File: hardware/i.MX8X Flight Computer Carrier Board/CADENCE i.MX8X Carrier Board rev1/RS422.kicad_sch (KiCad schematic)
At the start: 16 parts, among them CN1 DF11-16DP-2DSA(08), U18 MAX3485, U19 SN65C1168ERGYR, U20 P82B715DR

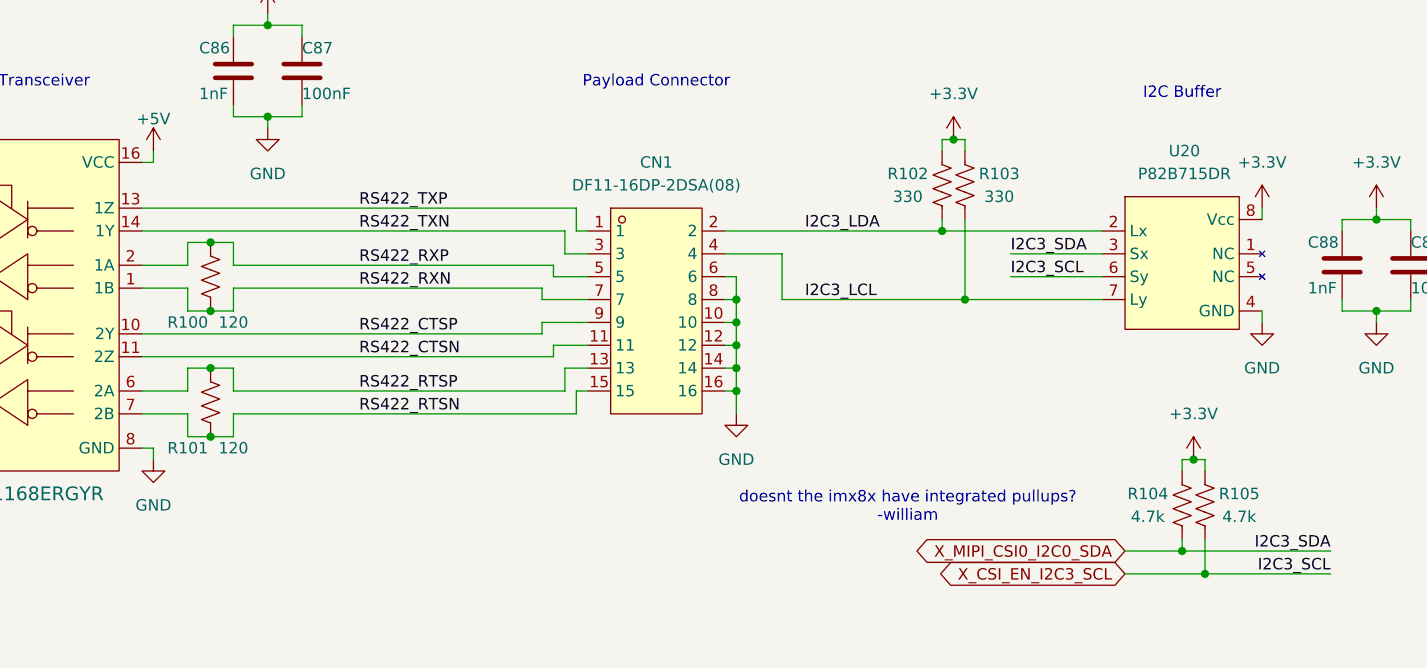
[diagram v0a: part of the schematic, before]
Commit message: Added pin definitions page
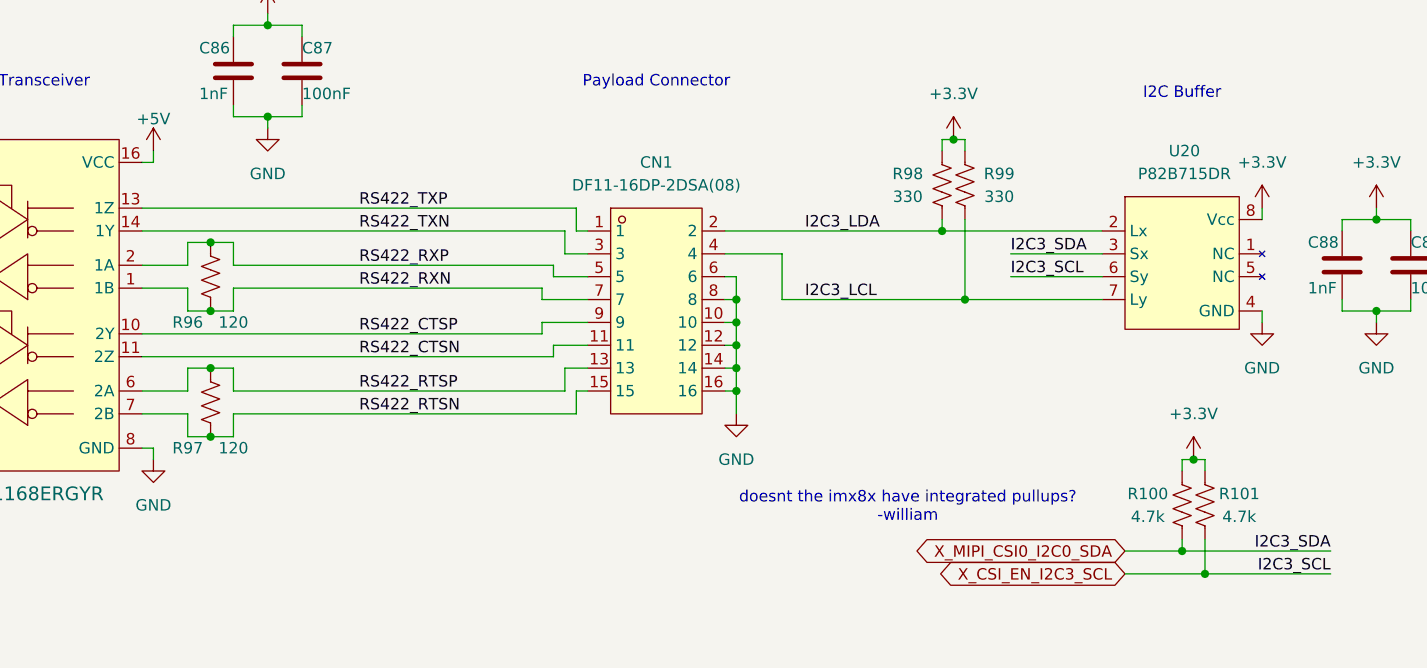
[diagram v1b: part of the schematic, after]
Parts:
- renumbered R104 to R100, R105 to R101, R100 to R96, R101 to R97, R102 to R98, R103 to R99
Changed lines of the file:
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@@
 		(on_board yes)
 		(dnp no)
-		(property "Reference" "R104"
+		(property "Reference" "R100"
 			(at 219.71 93.98 0)
 			(effects
@@
 			(project "CADENCE i.MX8X Carrier Board rev1"
 				(path "/de284495-d382-47cb-b528-76e440980d40/c0bf5d3f-4cfb-4c0b-b448-903517df1d5a"
-					(reference "R104")
+					(reference "R100")
 					(unit 1)
 				)
@@
 		(on_board yes)
 		(dnp no)
-		(property "Reference" "R101"
+		(property "Reference" "R97"
 			(at 113.03 88.9 0)
 			(effects
@@
 			(project "CADENCE i.MX8X Carrier Board rev1"
 				(path "/de284495-d382-47cb-b528-76e440980d40/c0bf5d3f-4cfb-4c0b-b448-903517df1d5a"
-					(reference "R101")
+					(reference "R97")
 					(unit 1)
 				)
@@
 		(on_board yes)
 		(dnp no)
-		(property "Reference" "#PWR0121"
+		(property "Reference" "#PWR0122"
 			(at 232.41 81.28 0)
 			(effects
@@
 			(project "CADENCE i.MX8X Carrier Board rev1"
 				(path "/de284495-d382-47cb-b528-76e440980d40/c0bf5d3f-4cfb-4c0b-b448-903517df1d5a"
-					(reference "#PWR0121")
+					(reference "#PWR0122")
 					(unit 1)
 				)
@@
 		(dnp no)
 		(fields_autoplaced yes)
-		(property "Reference" "#PWR0114"
+		(property "Reference" "#PWR0115"
 			(at 109.22 96.52 0)
 			(effects
@@
 			(project "CADENCE i.MX8X Carrier Board rev1"
 				(path "/de284495-d382-47cb-b528-76e440980d40/c0bf5d3f-4cfb-4c0b-b448-903517df1d5a"
-					(reference "#PWR0114")
+					(reference "#PWR0115")
 					(unit 1)
 				)
@@
 		(dnp no)
 		(fields_autoplaced yes)
-		(property "Reference" "#PWR0123"
+		(property "Reference" "#PWR0124"
 			(at 245.11 81.28 0)
 			(effects
@@
 			(project "CADENCE i.MX8X Carrier Board rev1"
 				(path "/de284495-d382-47cb-b528-76e440980d40/c0bf5d3f-4cfb-4c0b-b448-903517df1d5a"
-					(reference "#PWR0123")
+					(reference "#PWR0124")
 					(unit 1)
 				)
@@
 		(on_board yes)
 		(dnp no)
-		(property "Reference" "R100"
+		(property "Reference" "R96"
 			(at 113.03 74.93 0)
 			(effects
@@
 			(project "CADENCE i.MX8X Carrier Board rev1"
 				(path "/de284495-d382-47cb-b528-76e440980d40/c0bf5d3f-4cfb-4c0b-b448-903517df1d5a"
-					(reference "R100")
+					(reference "R96")
 					(unit 1)
 				)
@@
 		(on_board yes)
 		(dnp no)
-		(property "Reference" "R103"
+		(property "Reference" "R99"
 			(at 203.2 58.42 0)
 			(effects
@@
 			(project "CADENCE i.MX8X Carrier Board rev1"
 				(path "/de284495-d382-47cb-b528-76e440980d40/c0bf5d3f-4cfb-4c0b-b448-903517df1d5a"
-					(reference "R103")
+					(reference "R99")
 					(unit 1)
 				)
@@
 		(dnp no)
 		(fields_autoplaced yes)
-		(property "Reference" "#PWR0109"
+		(property "Reference" "#PWR0110"
 			(at -191.77 102.87 0)
 			(effects
@@
 			(project "CADENCE i.MX8X Carrier Board rev1"
 				(path "/de284495-d382-47cb-b528-76e440980d40/c0bf5d3f-4cfb-4c0b-b448-903517df1d5a"
-					(reference "#PWR0109")
+					(reference "#PWR0110")
 					(unit 1)
 				)
@@
 		(dnp no)
 		(fields_autoplaced yes)
-		(property "Reference" "#PWR0115"
+		(property "Reference" "#PWR0116"
 			(at 121.92 44.45 0)
 			(effects
@@
 			(project "CADENCE i.MX8X Carrier Board rev1"
 				(path "/de284495-d382-47cb-b528-76e440980d40/c0bf5d3f-4cfb-4c0b-b448-903517df1d5a"
-					(reference "#PWR0115")
+					(reference "#PWR0116")
 					(unit 1)
 				)
@@
 		(dnp no)
 		(fields_autoplaced yes)
-		(property "Reference" "#PWR0118"
+		(property "Reference" "#PWR0119"
 			(at 198.12 58.42 0)
 			(effects
@@
 			(project "CADENCE i.MX8X Carrier Board rev1"
 				(path "/de284495-d382-47cb-b528-76e440980d40/c0bf5d3f-4cfb-4c0b-b448-903517df1d5a"
-					(reference "#PWR0118")
+					(reference "#PWR0119")
 					(unit 1)
 				)
@@
 		(on_board yes)
 		(dnp no)
-		(property "Reference" "R102"
+		(property "Reference" "R98"
 			(at 193.04 58.42 0)
 			(effects
@@
 			(project "CADENCE i.MX8X Carrier Board rev1"
 				(path "/de284495-d382-47cb-b528-76e440980d40/c0bf5d3f-4cfb-4c0b-b448-903517df1d5a"
-					(reference "R102")
+					(reference "R98")
 					(unit 1)
 				)
@@
 		(dnp no)
 		(fields_autoplaced yes)
-		(property "Reference" "#PWR0122"
+		(property "Reference" "#PWR0123"
 			(at 245.11 66.04 0)
 			(effects
@@
 			(project "CADENCE i.MX8X Carrier Board rev1"
 				(path "/de284495-d382-47cb-b528-76e440980d40/c0bf5d3f-4cfb-4c0b-b448-903517df1d5a"
-					(reference "#PWR0122")
+					(reference "#PWR0123")
 					(unit 1)
 				)
@@
 		(dnp no)
 		(fields_autoplaced yes)
-		(property "Reference" "#PWR0117"
+		(property "Reference" "#PWR0118"
 			(at 173.99 91.44 0)
 			(effects
@@
 			(project "CADENCE i.MX8X Carrier Board rev1"
 				(path "/de284495-d382-47cb-b528-76e440980d40/c0bf5d3f-4cfb-4c0b-b448-903517df1d5a"
-					(reference "#PWR0117")
+					(reference "#PWR0118")
 					(unit 1)
 				)
@@
 		(dnp no)
 		(fields_autoplaced yes)
-		(property "Reference" "#PWR0120"
+		(property "Reference" "#PWR0121"
 			(at 232.41 66.04 0)
 			(effects
@@
 			(project "CADENCE i.MX8X Carrier Board rev1"
 				(path "/de284495-d382-47cb-b528-76e440980d40/c0bf5d3f-4cfb-4c0b-b448-903517df1d5a"
-					(reference "#PWR0120")
+					(reference "#PWR0121")
 					(unit 1)
 				)
@@
 		(on_board yes)
 		(dnp no)
-		(property "Reference" "#PWR0110"
+		(property "Reference" "#PWR0111"
 			(at -191.77 139.7 0)
 			(effects
@@
 			(project "CADENCE i.MX8X Carrier Board rev1"
 				(path "/de284495-d382-47cb-b528-76e440980d40/c0bf5d3f-4cfb-4c0b-b448-903517df1d5a"
-					(reference "#PWR0110")
+					(reference "#PWR0111")
 					(unit 1)
 				)
@@
 		(on_board yes)
 		(dnp no)
-		(property "Reference" "R105"
+		(property "Reference" "R101"
 			(at 229.87 93.98 0)
 			(effects
@@
 			(project "CADENCE i.MX8X Carrier Board rev1"
 				(path "/de284495-d382-47cb-b528-76e440980d40/c0bf5d3f-4cfb-4c0b-b448-903517df1d5a"
-					(reference "R105")
+					(reference "R101")
 					(unit 1)
 				)
@@
 		(on_board yes)
 		(dnp no)
-		(property "Reference" "#PWR0111"
+		(property "Reference" "#PWR0112"
 			(at 76.2 59.69 0)
 			(effects
@@
 			(project "CADENCE i.MX8X Carrier Board rev1"
 				(path "/de284495-d382-47cb-b528-76e440980d40/c0bf5d3f-4cfb-4c0b-b448-903517df1d5a"
-					(reference "#PWR0111")
+					(reference "#PWR0112")
 					(unit 1)
 				)
@@
 		(dnp no)
 		(fields_autoplaced yes)
-		(property "Reference" "#PWR0112"
+		(property "Reference" "#PWR0113"
 			(at 77.47 96.52 0)
 			(effects
@@
 			(project "CADENCE i.MX8X Carrier Board rev1"
 				(path "/de284495-d382-47cb-b528-76e440980d40/c0bf5d3f-4cfb-4c0b-b448-903517df1d5a"
-					(reference "#PWR0112")
+					(reference "#PWR0113")
 					(unit 1)
 				)
@@
 		(on_board yes)
 		(dnp no)
-		(property "Reference" "#PWR0113"
+		(property "Reference" "#PWR0114"
 			(at 109.22 59.69 0)
 			(effects
@@
 			(project "CADENCE i.MX8X Carrier Board rev1"
 				(path "/de284495-d382-47cb-b528-76e440980d40/c0bf5d3f-4cfb-4c0b-b448-903517df1d5a"
-					(reference "#PWR0113")
+					(reference "#PWR0114")
 					(unit 1)
 				)
@@
 		(dnp no)
 		(fields_autoplaced yes)
-		(property "Reference" "#PWR0116"
+		(property "Reference" "#PWR0117"
 			(at 121.92 59.69 0)
 			(effects
@@
 			(project "CADENCE i.MX8X Carrier Board rev1"
 				(path "/de284495-d382-47cb-b528-76e440980d40/c0bf5d3f-4cfb-4c0b-b448-903517df1d5a"
-					(reference "#PWR0116")
+					(reference "#PWR0117")
 					(unit 1)
 				)
@@
 		(on_board yes)
 		(dnp no)
-		(property "Reference" "#PWR0119"
+		(property "Reference" "#PWR0120"
 			(at 224.79 93.98 0)
 			(effects
@@
 			(project "CADENCE i.MX8X Carrier Board rev1"
 				(path "/de284495-d382-47cb-b528-76e440980d40/c0bf5d3f-4cfb-4c0b-b448-903517df1d5a"
-					(reference "#PWR0119")
-					(unit 1)
-				)
+					(reference "#PWR0120")
+					(unit 1)
+				)

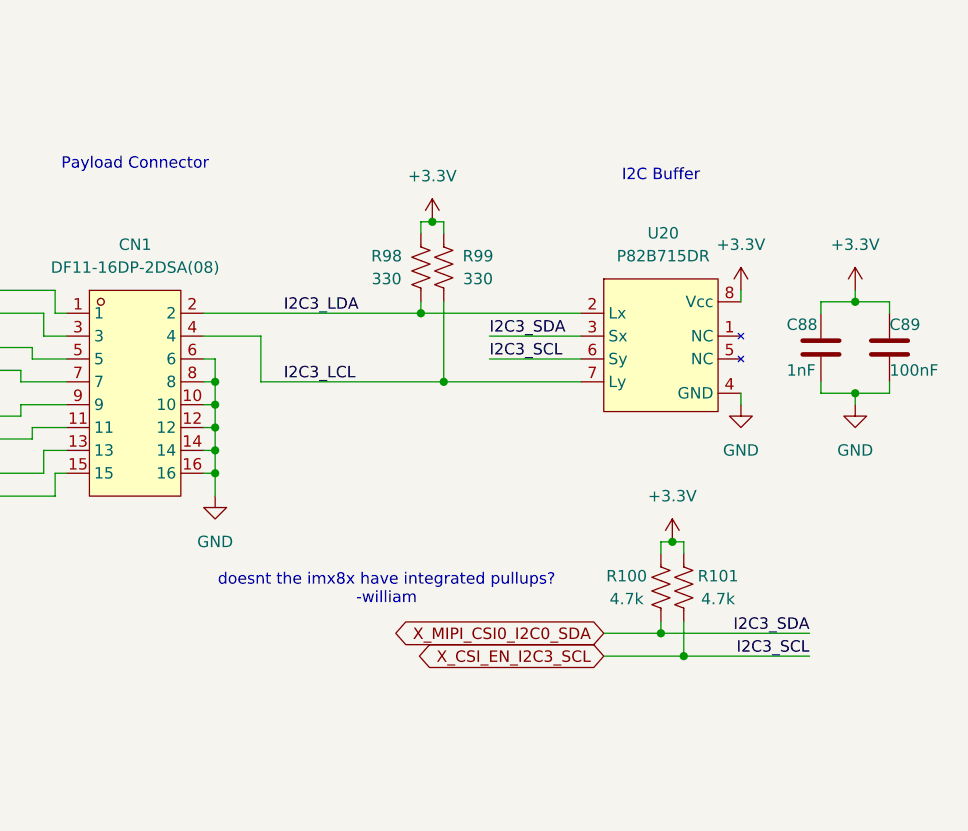
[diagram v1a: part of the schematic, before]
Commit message: Edited a lot based on IMX8x pin muxing tool
- validated watchdog pin
- edited some i2c definitions
- finally updated peripheral connections
- realized that UART0 needed to be reserved for programming flash directly, so routed it to FTDI and added a MUX to have a user selectable UART0 between FTDI and pin header
- shifted around UART 1, 2, and 3 as a result of above realization
- added gpio and level shifters for payload
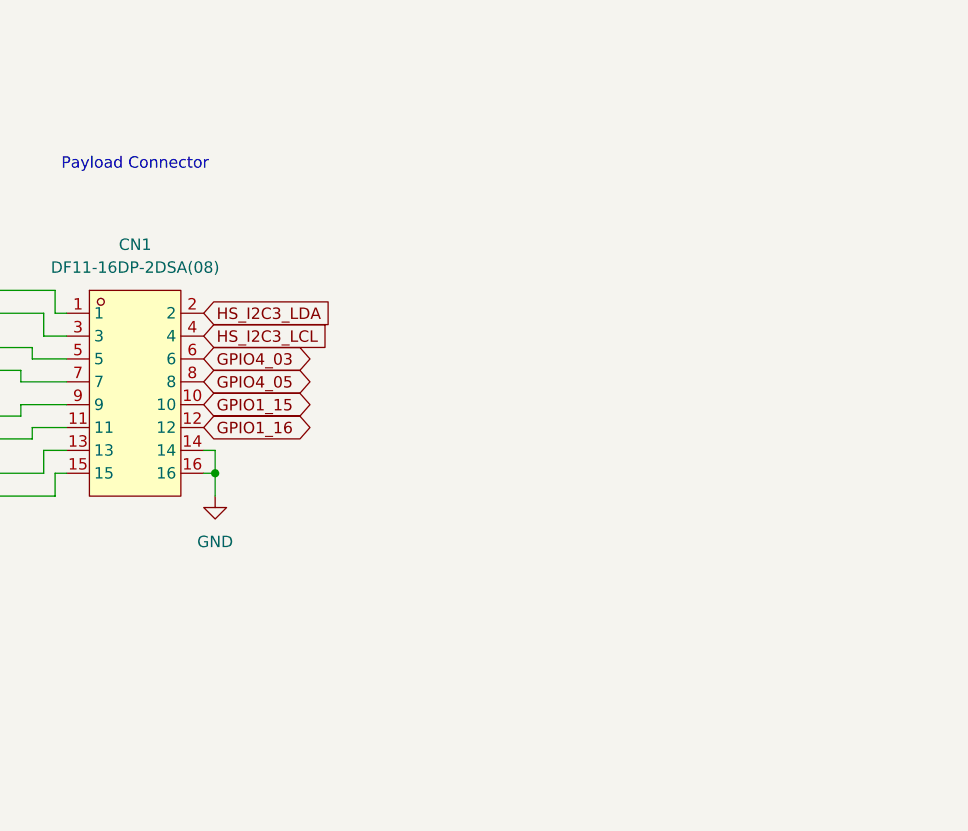
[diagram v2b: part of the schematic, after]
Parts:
- removed C88: 1nF, symbol Device:C
- removed C89: 100nF, symbol Device:C
- removed R100, R101: 4.7k, Resistor_SMD:R_0402_1005Metric, symbol Device:R_US
- removed R98, R99: 330, Resistor_SMD:R_0402_1005Metric, symbol Device:R_US
- removed U20: P82B715DR, symbol cadence carrier custom symbols:TI_P82B715DR
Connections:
- net GND: no longer CN1.10, CN1.12, CN1.6, CN1.8
- net I2C3_LCL renamed HS_I2C3_LCL
- net I2C3_LDA renamed HS_I2C3_LDA
- new net GPIO1_15: CN1.10
- new net GPIO1_16: CN1.12
- new net GPIO4_03: CN1.6
- new net GPIO4_05: CN1.8
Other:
- note removed: "I2C Buffer"
- note removed: "doesnt the imx8x have integrated pullups? -william"

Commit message: updated imx8x footprints
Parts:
- C86, C87: footprint (none) -> Capacitor_SMD:C_0603_1608Metric
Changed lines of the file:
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@@
 			)
 		)
-		(property "Footprint" ""
+		(property "Footprint" "Capacitor_SMD:C_0603_1608Metric"
 			(at 119.0752 50.8 0)
 			(effects
@@
 			)
 		)
-		(property "Footprint" ""
+		(property "Footprint" "Capacitor_SMD:C_0603_1608Metric"
 			(at 126.6952 50.8 0)
 			(effects
